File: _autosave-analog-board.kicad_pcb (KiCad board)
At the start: 2 copper layers, 200 x 150 mm, 488 parts, among them J1 AC IN, J2 OUT, J3 CONN_20X2, P2 CONN_01X02, Q1 2N3906, Q10 2N3906, Q11 2N3906, Q12 2N3906, Q13 2N3906, Q14 2N3906, Q15 2N3906, Q16 2N3906, Q17 NPN, Q18 NPN, Q19 J111, Q2 2N3906, Q20 2N3906, Q3 2N3906, Q4 2N3906, Q5 2N3906, Q6 BCM857BS, Q7 2N3906, Q8 2N3906, Q9 2N3906, U1 LM13700, U10 ADR01, U11 DG212B, U12 DG212B, U13 DG408, U14 DG408, U15 TL072-, U16 DG408, U17 DG408, U18 LM13700, U19 LM13700, U2 LM13700, U21 TL072-, U22 TL074-, U23 TL074-, U24 TL074-, U25 TL074-, U26 TL072-, U27 TL074-, U28 TL074-, U29 LM13700, U3 LM13700, U30 LM13700, U31 TL074-, U32 LM13700, U33 TL074-, U34 TL074-, U35 TL074-, U36 74LV573, U38 0 - 10V, U39 TL074-, U4 DG212B, U40 DG419, U41 0 - 10V, U42 10 - 0V, U43 LM7812, U44 LM7912, U45 DG408, U46 7805, U5 TL074-, U6 AD5556, U7 TL072-, U8 TL074-, U9 AD8672

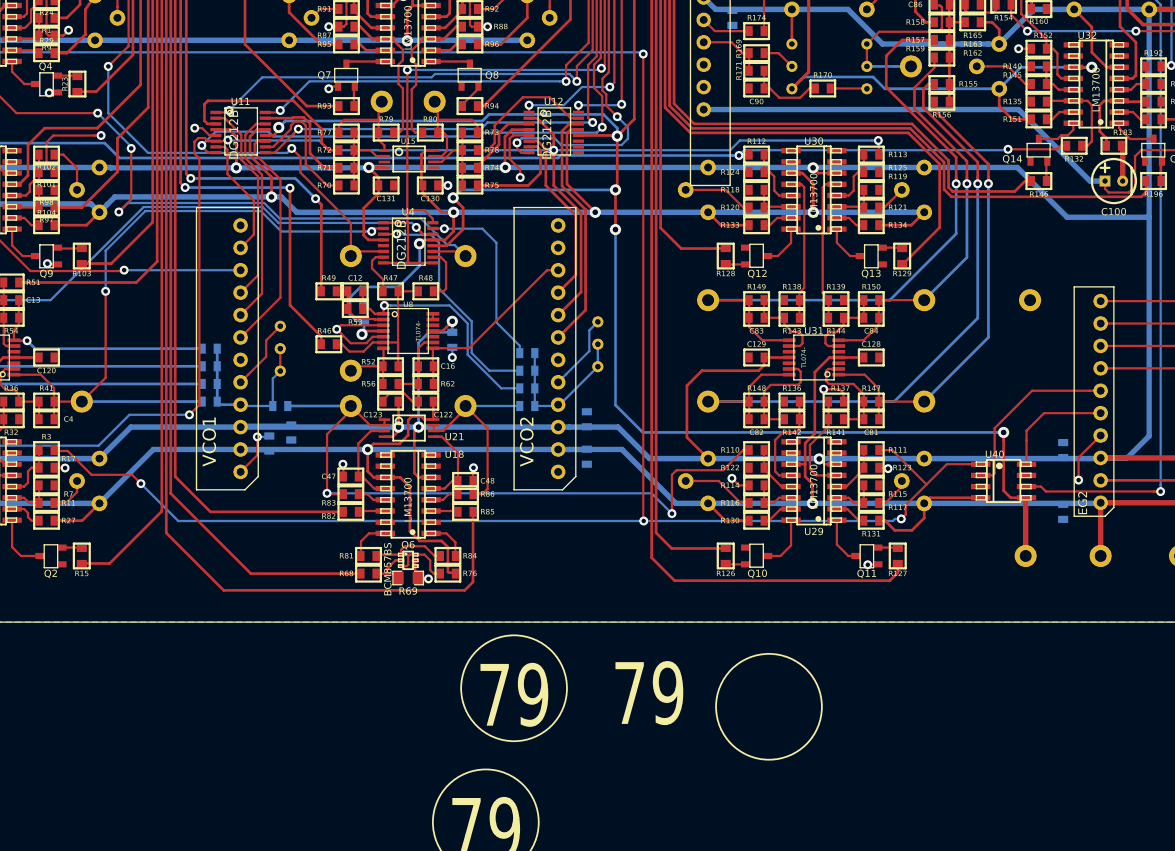
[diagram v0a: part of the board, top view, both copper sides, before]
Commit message: adding external CV and GATE input test points
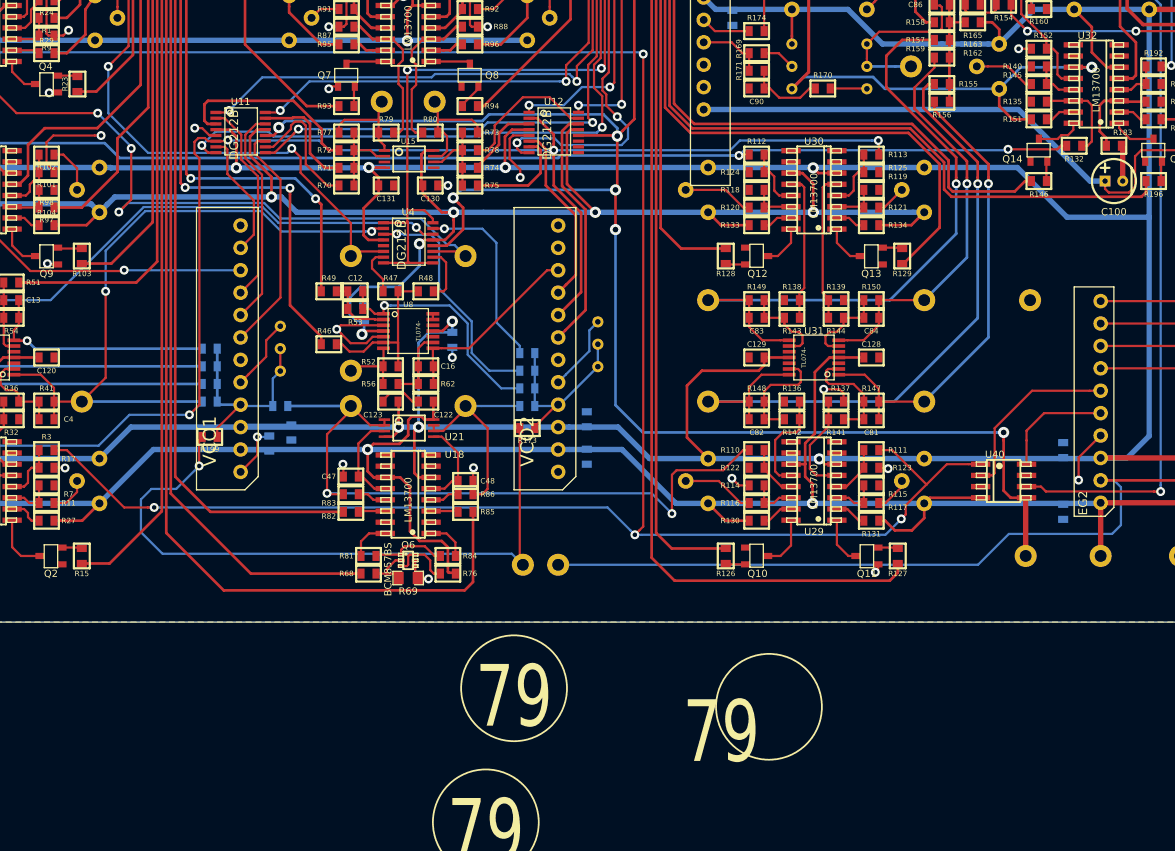
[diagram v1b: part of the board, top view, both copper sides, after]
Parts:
- added R173: 100K, MyModules:SM0603-R-JRL, F.Cu at (86.5, 128.0)
- added R199: 100K, MyModules:SM0603-R-JRL, F.Cu at (50.5, 129.0)
- added TP38: CONN_1, MyModules:TEST POINT, B.Cu at (86.0, 143.5)
- added TP39: CONN_1, MyModules:TEST POINT, B.Cu at (90.0, 143.5)
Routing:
- net EXT_CV_IN: track 0.00 -> 75.8 mm, vias 0 -> 1
- net GATE: track 159.8 -> 232.4 mm
- net Net-(R199-Pad1): track 19.4 -> 24.1 mm
- net Net-(R173-Pad1): track 17.5 -> 21.4 mm
- net EG2: track 261.0 -> 264.2 mm
